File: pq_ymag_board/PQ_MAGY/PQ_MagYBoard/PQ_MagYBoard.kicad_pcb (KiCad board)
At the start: 6 copper layers, 45 x 45 mm, 10 parts, among them J1 M20-7810245

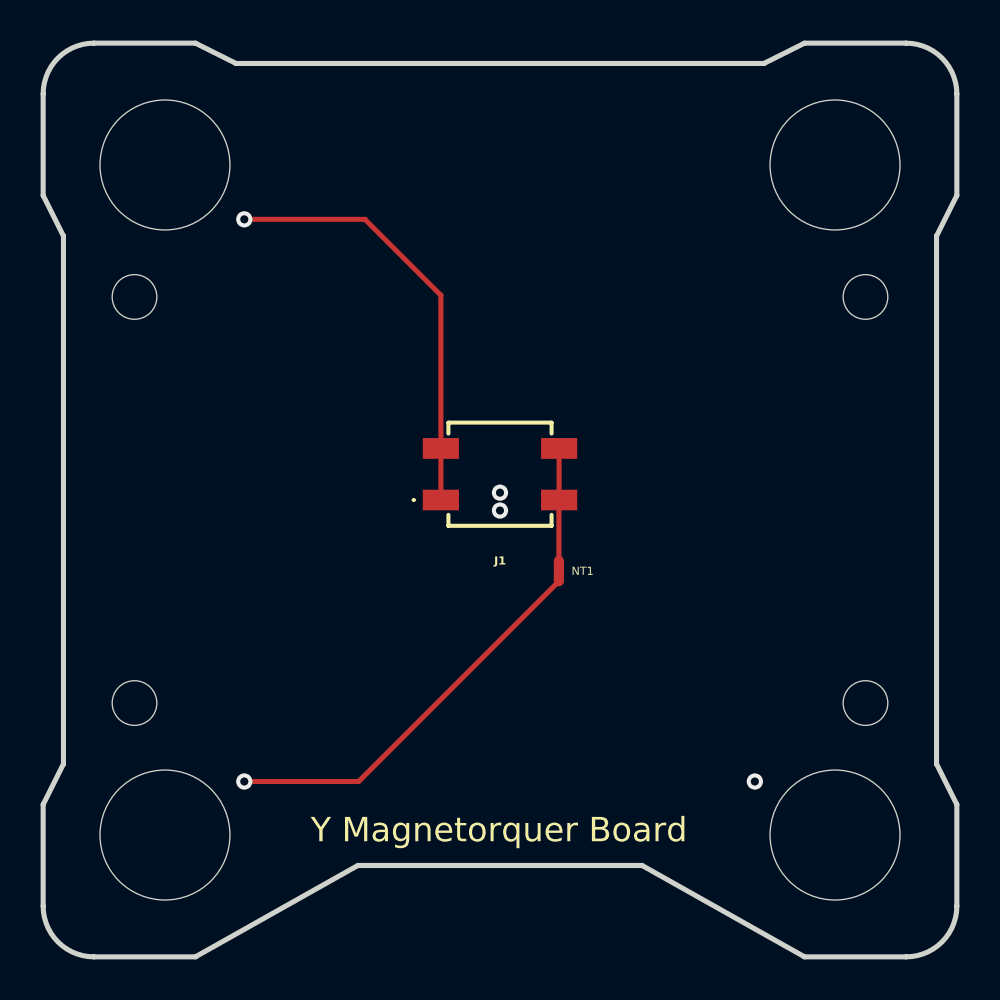
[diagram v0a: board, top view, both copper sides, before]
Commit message: Add names of PQ collaborators in Y magnetorquer
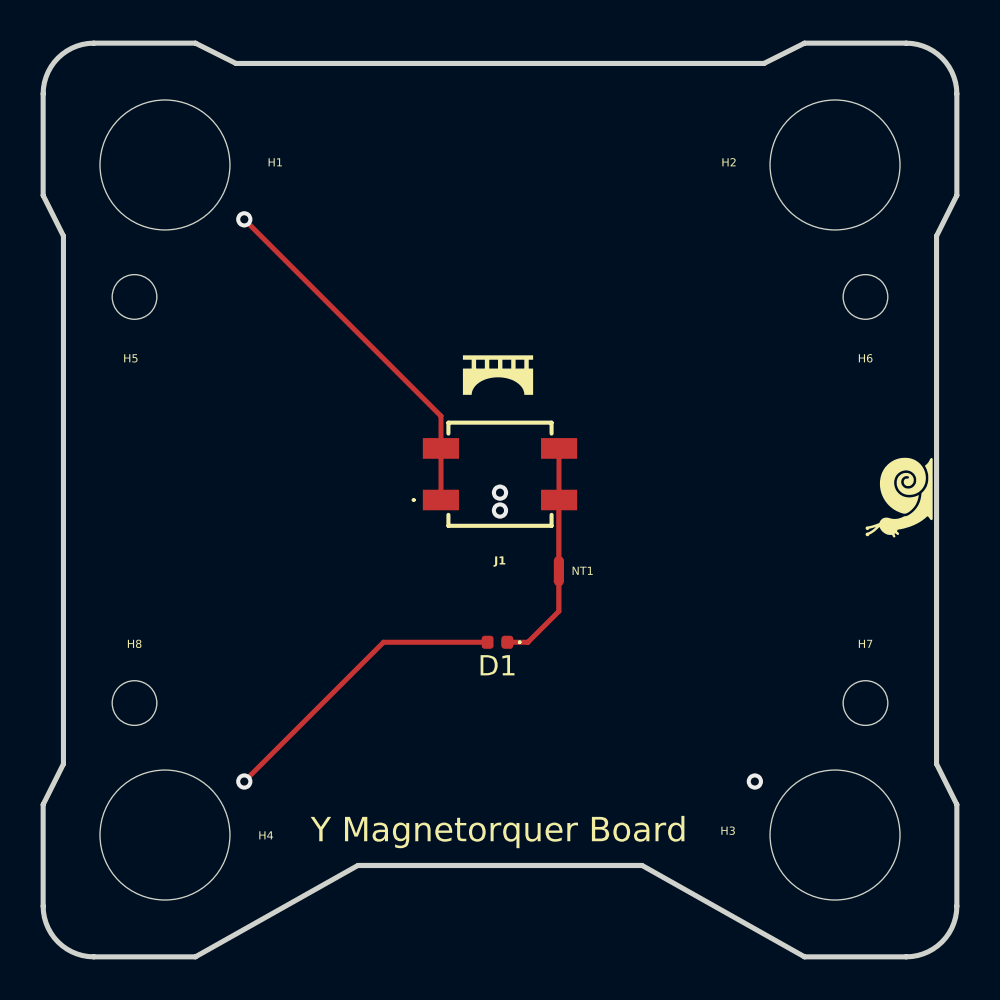
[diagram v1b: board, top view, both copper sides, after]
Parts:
- added Annotation1: Bridgemaker, -nsl_symbols:Bridgemaker, F.Cu at (101.6, 54.7)
- added Annotation3: snail, snail:v2, F.Cu at (121.4, 60.6)
- added D1: LED, LED_SMD:LED_0402_1005Metric, F.Cu at (101.6, 67.8)
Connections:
- NT1 pad 1: /VCC_MAG -> Net-(D1-K)
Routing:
- net /VCC_MAG: track 6370.0 -> 6361.8 mm
- net Net-(D1-K): track 0.00 -> 4.65 mm
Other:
- board text added: "Adriano Camps Carmona Luis Contreras Benito Amadeu Gonga Siles Guillem Gràcia I Solà"
- board text added: "Albert Arnau Roger Bock Gerard Bou Claudia Bracons Lydia Campos Oriol Cancio Marc Cordero Miguel Diaz Youssef El Kaisi George Vlad Jose Manuel Esbrí Abderrahman Ettahrioui Albert Fàbregas Jose Faneca Oriol Ferrer David Fornós Albert Garcia Iker Garcia Guillem Gibert Pol Giménez Daniel Herencia Pere Hernández Alex Hernández Pau Jiménez Leixin Jin Salvatore Lombardi Eric Maldonado"
- board text added: "David Llavería Godoy Adrián Pérez Portero Stefan Podaru Joan Adrià Ruiz de Azúa"
- board text added: "Enric Martin Sergio Mateo Alex Meléndez Àlex Mitjans Robert Molina Adrià Molló Xavier Morales Ainna Yue Moreno Jaume Motjé Sergio Muñoz Mireia Nogué Alexandre Perea Oriol Picart David Reiss de Fez Antonio Romero Nil Rius Rubén Ruíz Guifré Sala Carlos Daniel Salvadó Pol Simon Sebastian Skit Erik Solé Júlia Tribó Martina Tucci Marti Xagaray Igor Yuziv Edison Gabriel Zaragosin"
- board text added: "IEEE Open PocketQube Kit"

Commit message: Removed netie, reordered names, added diacritics, added NSL hexagonal logo
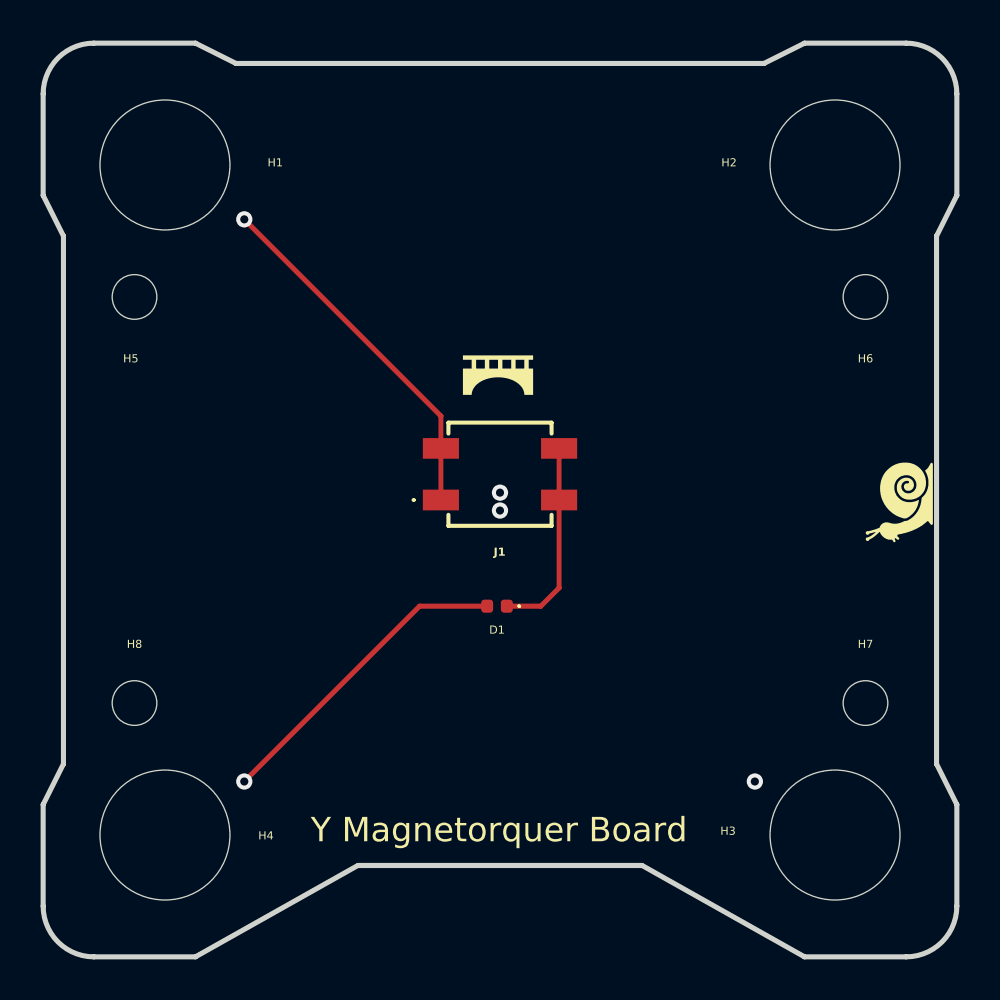
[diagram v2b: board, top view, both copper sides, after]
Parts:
- removed NT1: NetTie_2, NetTie:NetTie-2_SMD_Pad0.5mm
- added Annotation2: NSL_hexagon, symbols-nsl:NSL_hexagon, B.Cu at (101.7, 59.6)
- Annotation1: footprint -nsl_symbols:Bridgemaker -> symbols-nsl:Bridgemaker
- Annotation3: footprint snail:v2 -> symbols-nsl:Snail
- J1: footprint -nsl_connector:M207810245 -> connector-nsl:M207810245
- moved D1 1.78 mm to (101.6, 66.0)
- moved Annotation3 0.67 mm to (121.8, 60.1)
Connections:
- D1 pad 1: Net-(D1-K) -> /MAG+Y
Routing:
- net Net-(D1-K): track 4.65 -> 0.00 mm
- net /MAG+Y: track 5.54 -> 9.83 mm
- net /VCC_MAG: track 6361.8 -> 6362.5 mm
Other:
- board text added: "Adriano Camps Carmona Ștefan Podaru Amadeu Gonga Siles Luis Contreras Benito Nil Rius Fortuny"
- board text added: "Albert Arnau Arnau Dolz Claudia Bracons Vlad Enache Leixin Jin Antonio Romero Guifré Sala Guillem Gilbert Pol Giménez Daniel Herencia Robert Molina Gerard Bou Marc Cordero Roger Bock Jose Esbrí Iker Garcia Salvatore Lombardi Martina Tucci Ainna Moreno Mireia Nogué Edison Zaragosin Roger Almirall Abderrahman Ettahrioui Albert Fàbregas David Fornós Sergio Mateo Alex Meléndez Xavier Morales"
- board text added: "David Llavería Godoy Guillem Gràcia I Solà Adrián Pérez Portero Joan Adrià Ruiz de Azúa Júlia Tribó Cabré"
- board text added: "Oriol Picart Carlos Salvadó Martí Xargay Lydia Campos Jose Faneca Pere Hernández Pau Jiménez Youssef El Kaisi Àlex Mitjans Adrià Molló Alexandre Perea Rubén Ruíz Erik Solé Alex Hernández Edgar Hernández Artur Cot Sergio Muñoz Vladimir Frunză Eric Maldonado Oriol Cancio Oriol Ferrer Albert Garcia Enric Martin Eric Maldonado Sebastian Skit Igor Yuziv Jaume Motjé David Reiss"
- board text removed: "Adriano Camps Carmona Luis Contreras Benito Amadeu Gonga Siles Guillem Gràcia I Solà"
- board text removed: "Albert Arnau Roger Bock Gerard Bou Claudia Bracons Lydia Campos Oriol Cancio Marc Cordero Miguel Diaz Youssef El Kaisi George Vlad Jose Manuel Esbrí Abderrahman Ettahrioui Albert Fàbregas Jose Faneca Oriol Ferrer David Fornós Albert Garcia Iker Garcia Guillem Gibert Pol Giménez Daniel Herencia Pere Hernández Alex Hernández Pau Jiménez Leixin Jin Salvatore Lombardi Eric Maldonado"
- board text removed: "David Llavería Godoy Adrián Pérez Portero Stefan Podaru Joan Adrià Ruiz de Azúa"
- board text removed: "Enric Martin Sergio Mateo Alex Meléndez Àlex Mitjans Robert Molina Adrià Molló Xavier Morales Ainna Yue Moreno Jaume Motjé Sergio Muñoz Mireia Nogué Alexandre Perea Oriol Picart David Reiss de Fez Antonio Romero Nil Rius Rubén Ruíz Guifré Sala Carlos Daniel Salvadó Pol Simon Sebastian Skit Erik Solé Júlia Tribó Martina Tucci Marti Xagaray Igor Yuziv Edison Gabriel Zaragosin"
